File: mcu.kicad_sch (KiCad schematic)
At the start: 15 parts, among them U3 STM32L431CBT6

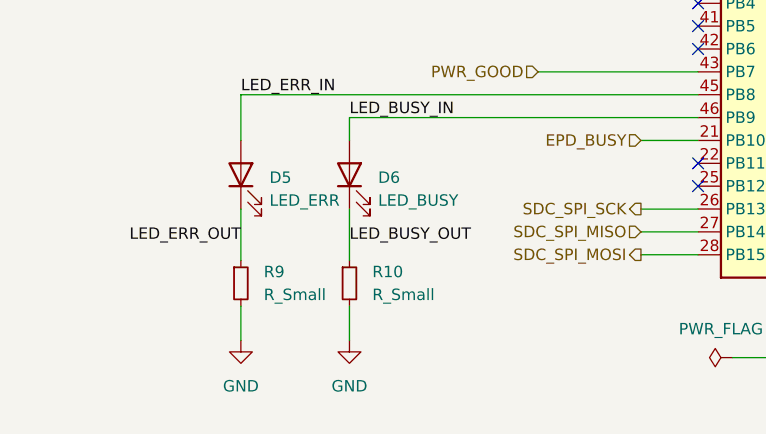
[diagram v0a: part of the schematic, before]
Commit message: Added footprint for components in Schematics. Updated LED resistors
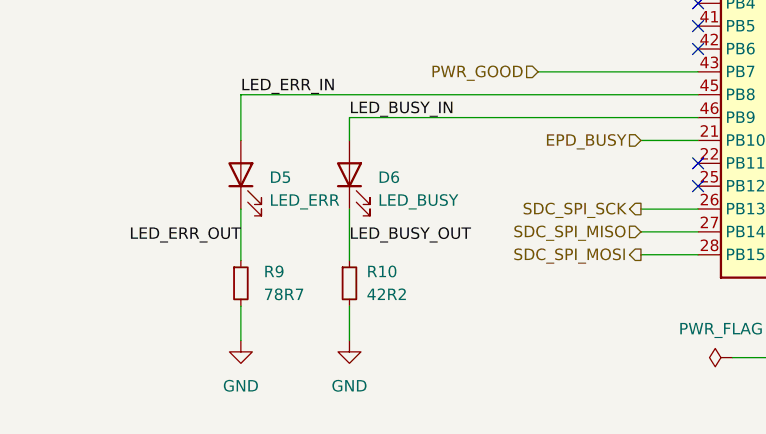
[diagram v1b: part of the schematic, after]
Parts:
- C37, C38, C39, C40, C41, C42, C43, C44: footprint (none) -> Capacitor_SMD:C_0201_0603Metric
- D5, D6: footprint (none) -> LED_THT:LED_D3.0mm
- L4: footprint (none) -> Inductor_SMD:L_0402_1005Metric
- R10: value R_Small -> 42R2; footprint (none) -> Resistor_SMD:R_1210_3225Metric
- R11: footprint (none) -> Resistor_SMD:R_0805_2012Metric
- R9: value R_Small -> 78R7; footprint (none) -> Resistor_SMD:R_1210_3225Metric
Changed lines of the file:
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@@
       (effects (font (size 1.27 1.27)) (justify left))
     )
-    (property "Footprint" "" (id 2) (at 143.51 40.64 0)
+    (property "Footprint" "Capacitor_SMD:C_0201_0603Metric" (id 2) (at 143.51 40.64 0)
       (effects (font (size 1.27 1.27)) hide)
     )
@@
       (effects (font (size 1.27 1.27)) (justify left))
     )
-    (property "Value" "R_Small" (id 1) (at 80.01 141.6049 0)
-      (effects (font (size 1.27 1.27)) (justify left))
-    )
-    (property "Footprint" "" (id 2) (at 77.47 140.335 0)
+    (property "Value" "78R7" (id 1) (at 80.01 141.6049 0)
+      (effects (font (size 1.27 1.27)) (justify left))
+    )
+    (property "Footprint" "Resistor_SMD:R_1210_3225Metric" (id 2) (at 77.47 140.335 0)
       (effects (font (size 1.27 1.27)) hide)
     )
@@
       (effects (font (size 1.27 1.27)) (justify left))
     )
-    (property "Footprint" "" (id 2) (at 110.49 40.64 0)
+    (property "Footprint" "Capacitor_SMD:C_0201_0603Metric" (id 2) (at 110.49 40.64 0)
       (effects (font (size 1.27 1.27)) hide)
     )
@@
       (effects (font (size 1.27 1.27)) (justify right))
     )
-    (property "Footprint" "" (id 2) (at 89.535 128.27 0)
+    (property "Footprint" "LED_THT:LED_D3.0mm" (id 2) (at 89.535 128.27 0)
       (effects (font (size 1.27 1.27)) hide)
     )
@@
       (effects (font (size 1.27 1.27)) (justify left))
     )
-    (property "Footprint" "" (id 2) (at 184.15 38.1 0)
+    (property "Footprint" "Capacitor_SMD:C_0201_0603Metric" (id 2) (at 184.15 38.1 0)
       (effects (font (size 1.27 1.27)) hide)
     )
@@
       (effects (font (size 1.27 1.27)) (justify right))
     )
-    (property "Footprint" "" (id 2) (at 77.47 128.27 0)
+    (property "Footprint" "LED_THT:LED_D3.0mm" (id 2) (at 77.47 128.27 0)
       (effects (font (size 1.27 1.27)) hide)
     )
@@
       (effects (font (size 1.27 1.27)) (justify left))
     )
-    (property "Footprint" "" (id 2) (at 132.08 40.64 0)
+    (property "Footprint" "Capacitor_SMD:C_0201_0603Metric" (id 2) (at 132.08 40.64 0)
       (effects (font (size 1.27 1.27)) hide)
     )
@@
       (effects (font (size 1.27 1.27)) (justify left))
     )
-    (property "Footprint" "" (id 2) (at 154.94 40.64 0)
+    (property "Footprint" "Capacitor_SMD:C_0201_0603Metric" (id 2) (at 154.94 40.64 0)
       (effects (font (size 1.27 1.27)) hide)
     )
@@
   (symbol (lib_id "Device:R_Small") (at 89.535 140.335 0) (unit 1)
     (in_bom yes) (on_board yes) (fields_autoplaced)
-    (property "Reference" "R10" (id 0) (at 92.075 139.0649 0)
-      (effects (font (size 1.27 1.27)) (justify left))
-    )
-    (property "Value" "R_Small" (id 1) (at 92.075 141.6049 0)
-      (effects (font (size 1.27 1.27)) (justify left))
-    )
-    (property "Footprint" "" (id 2) (at 89.535 140.335 0)
+    (property "Reference" "R10" (id 0) (at 91.44 139.0649 0)
+      (effects (font (size 1.27 1.27)) (justify left))
+    )
+    (property "Value" "42R2" (id 1) (at 91.44 141.6049 0)
+      (effects (font (size 1.27 1.27)) (justify left))
+    )
+    (property "Footprint" "Resistor_SMD:R_1210_3225Metric" (id 2) (at 89.535 140.335 0)
       (effects (font (size 1.27 1.27)) hide)
     )
@@
       (effects (font (size 1.27 1.27)) (justify left))
     )
-    (property "Footprint" "" (id 2) (at 101.6 88.265 0)
+    (property "Footprint" "Resistor_SMD:R_0805_2012Metric" (id 2) (at 101.6 88.265 0)
       (effects (font (size 1.27 1.27)) hide)
     )
@@
       (effects (font (size 1.27 1.27)) (justify left))
     )
-    (property "Footprint" "" (id 2) (at 120.65 40.64 0)
+    (property "Footprint" "Capacitor_SMD:C_0201_0603Metric" (id 2) (at 120.65 40.64 0)
       (effects (font (size 1.27 1.27)) hide)
     )
@@
       (effects (font (size 1.27 1.27)) (justify left))
     )
-    (property "Footprint" "" (id 2) (at 175.26 38.1 0)
+    (property "Footprint" "Capacitor_SMD:C_0201_0603Metric" (id 2) (at 175.26 38.1 0)
       (effects (font (size 1.27 1.27)) hide)
     )
@@
     (property "Reference" "L4" (id 0) (at 170.18 29.21 90))
     (property "Value" "39nH" (id 1) (at 170.18 31.75 90))
-    (property "Footprint" "" (id 2) (at 170.18 34.29 0)
+    (property "Footprint" "Inductor_SMD:L_0402_1005Metric" (id 2) (at 170.18 34.29 0)
       (effects (font (size 1.27 1.27)) hide)
     )
@@
       (effects (font (size 1.27 1.27)) (justify left))
     )
-    (property "Footprint" "" (id 2) (at 92.075 80.01 0)
-      (effects (font (size 1.27 1.27)) hide)
-    )
+    (property "Footprint" "Capacitor_SMD:C_0201_0603Metric" (id 2) (at 92.075 80.01 0)
+      (effects (font (size 1.27 1.27)) hide)
+    )

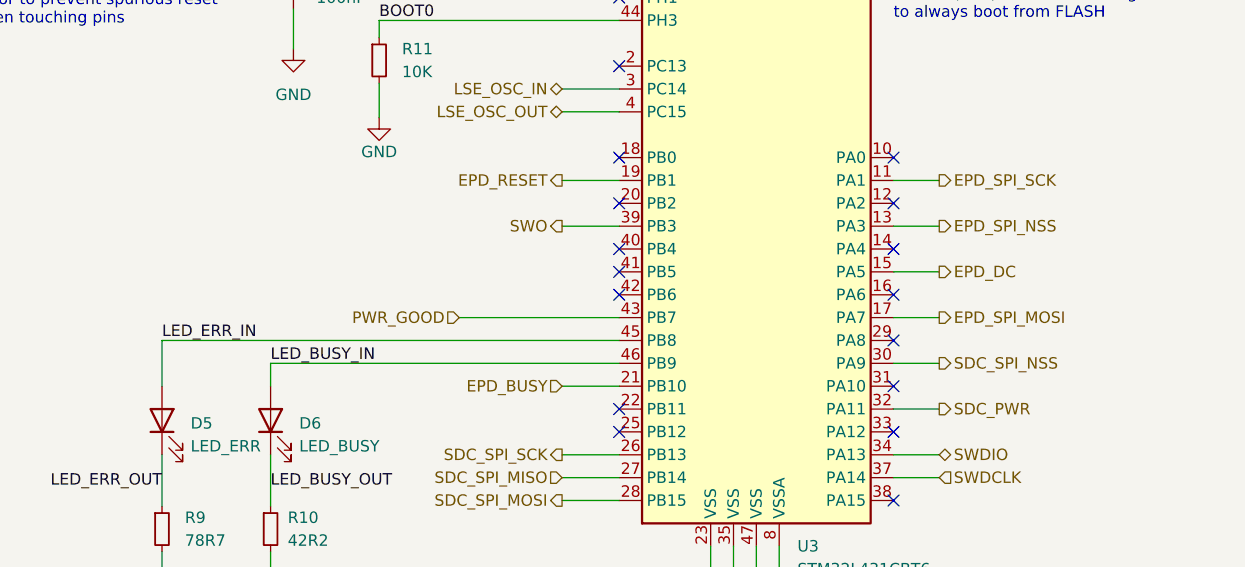
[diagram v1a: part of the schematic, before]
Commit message: Added preliminary PCL layout
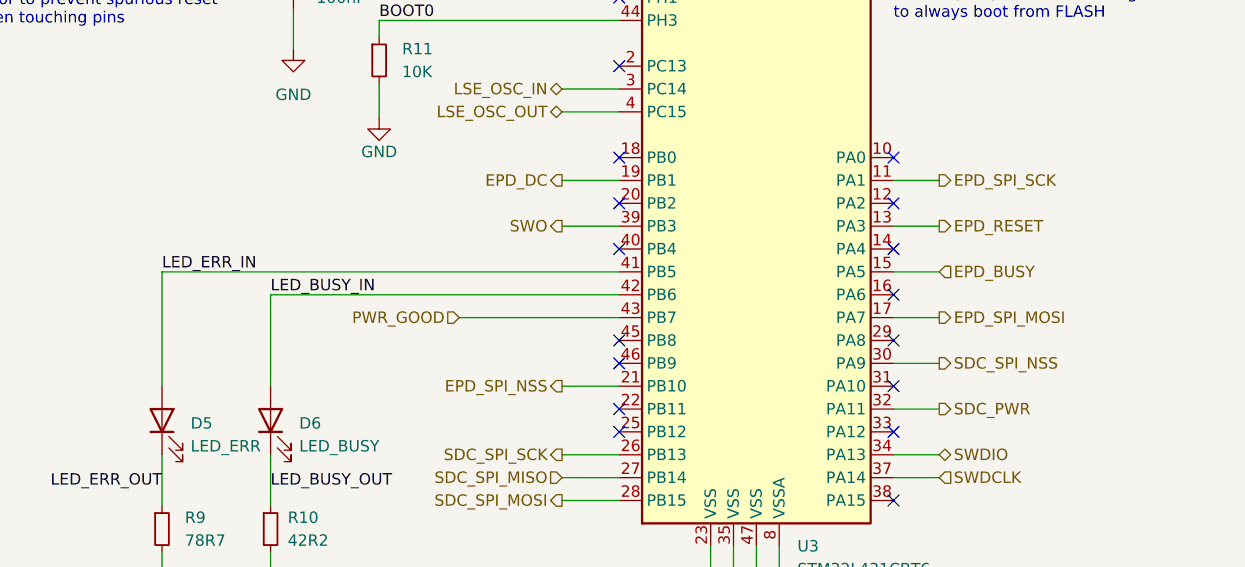
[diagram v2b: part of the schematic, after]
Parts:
- C37, C38, C39, C40, C41, C42, C43, C44: footprint Capacitor_SMD:C_0201_0603Metric -> Capacitor_SMD:C_0603_1608Metric
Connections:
- net EPD_BUSY: now also U3.15 (PA5); no longer U3.21 (PB10)
- net EPD_DC: now also U3.19 (PB1); no longer U3.15 (PA5)
- net EPD_RESET: now also U3.13 (PA3); no longer U3.19 (PB1)
- net EPD_SPI_NSS: now also U3.21 (PB10); no longer U3.13 (PA3)
- net LED_BUSY_IN: now also U3.42 (PB6); no longer U3.46 (PB9)
- net LED_ERR_IN: now also U3.41 (PB5); no longer U3.45 (PB8)
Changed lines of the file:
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@@
   (junction (at 140.97 146.05) (diameter 0) (color 0 0 0 0)
   )
+  (no_connect (at 128.27 121.92))
   (no_connect (at 158.75 129.54))
   (no_connect (at 128.27 99.06))
   (no_connect (at 128.27 129.54))
+  (no_connect (at 128.27 119.38))
   (no_connect (at 128.27 81.28))
   (no_connect (at 158.75 109.22))
@@
   (no_connect (at 158.75 119.38))
   (no_connect (at 128.27 88.9))
-  (no_connect (at 128.27 111.76))
-  (no_connect (at 128.27 114.3))
   (no_connect (at 128.27 127))
   (no_connect (at 128.27 109.22))
@@
     (stroke (width 0) (type default) (color 0 0 0 0))
   )
-  (wire (pts (xy 77.47 119.38) (xy 128.27 119.38))
+  (wire (pts (xy 77.47 111.76) (xy 128.27 111.76))
     (stroke (width 0) (type default) (color 0 0 0 0))
   )
@@
     (stroke (width 0) (type default) (color 0 0 0 0))
   )
-  (wire (pts (xy 89.535 121.92) (xy 128.27 121.92))
+  (wire (pts (xy 89.535 114.3) (xy 128.27 114.3))
     (stroke (width 0) (type default) (color 0 0 0 0))
   )
@@
     (stroke (width 0) (type default) (color 0 0 0 0))
   )
-  (wire (pts (xy 89.535 121.92) (xy 89.535 124.46))
+  (wire (pts (xy 89.535 114.3) (xy 89.535 124.46))
     (stroke (width 0) (type default) (color 0 0 0 0))
   )
@@
     (stroke (width 0) (type default) (color 0 0 0 0))
   )
-  (wire (pts (xy 77.47 119.38) (xy 77.47 124.46))
+  (wire (pts (xy 77.47 111.76) (xy 77.47 124.46))
     (stroke (width 0) (type default) (color 0 0 0 0))
   )
@@
     (effects (font (size 1.27 1.27)) (justify right bottom))
   )
-  (label "LED_ERR_IN" (at 77.47 119.38 0)
+  (label "LED_ERR_IN" (at 77.47 111.76 0)
     (effects (font (size 1.27 1.27)) (justify left bottom))
   )
@@
     (effects (font (size 1.27 1.27)) (justify left bottom))
   )
-  (label "LED_BUSY_IN" (at 89.535 121.92 0)
-    (effects (font (size 1.27 1.27)) (justify left bottom))
-  )
-  (hierarchical_label "EPD_SPI_NSS" (shape output) (at 163.83 106.68 0)
-    (effects (font (size 1.27 1.27)) (justify left))
+  (label "LED_BUSY_IN" (at 89.535 114.3 0)
+    (effects (font (size 1.27 1.27)) (justify left bottom))
+  )
+  (hierarchical_label "EPD_SPI_NSS" (shape output) (at 121.92 124.46 180)
+    (effects (font (size 1.27 1.27)) (justify right))
   )
   (hierarchical_label "SDC_SPI_NSS" (shape output) (at 163.83 121.92 0)
@@
     (effects (font (size 1.27 1.27)) (justify right))
   )
-  (hierarchical_label "EPD_RESET" (shape output) (at 121.92 101.6 180)
-    (effects (font (size 1.27 1.27)) (justify right))
-  )
-  (hierarchical_label "EPD_DC" (shape output) (at 163.83 111.76 0)
-    (effects (font (size 1.27 1.27)) (justify left))
+  (hierarchical_label "EPD_RESET" (shape output) (at 163.83 106.68 0)
+    (effects (font (size 1.27 1.27)) (justify left))
+  )
+  (hierarchical_label "EPD_DC" (shape output) (at 121.92 101.6 180)
+    (effects (font (size 1.27 1.27)) (justify right))
   )
   (hierarchical_label "SDC_SPI_MISO" (shape input) (at 121.92 134.62 180)
@@
     (effects (font (size 1.27 1.27)) (justify right))
   )
-  (hierarchical_label "EPD_BUSY" (shape input) (at 121.92 124.46 180)
-    (effects (font (size 1.27 1.27)) (justify right))
+  (hierarchical_label "EPD_BUSY" (shape input) (at 163.83 111.76 0)
+    (effects (font (size 1.27 1.27)) (justify left))
   )
   (symbol (lib_id "Device:C_Small") (at 143.51 40.64 0) (unit 1)
@@
       (effects (font (size 1.27 1.27)) (justify left))
     )
-    (property "Footprint" "Capacitor_SMD:C_0201_0603Metric" (id 2) (at 143.51 40.64 0)
+    (property "Footprint" "Capacitor_SMD:C_0603_1608Metric" (id 2) (at 143.51 40.64 0)
       (effects (font (size 1.27 1.27)) hide)
     )
@@
       (effects (font (size 1.27 1.27)) (justify left))
     )
-    (property "Footprint" "Capacitor_SMD:C_0201_0603Metric" (id 2) (at 110.49 40.64 0)
+    (property "Footprint" "Capacitor_SMD:C_0603_1608Metric" (id 2) (at 110.49 40.64 0)
       (effects (font (size 1.27 1.27)) hide)
     )
@@
       (effects (font (size 1.27 1.27)) (justify left))
     )
-    (property "Footprint" "Capacitor_SMD:C_0201_0603Metric" (id 2) (at 184.15 38.1 0)
+    (property "Footprint" "Capacitor_SMD:C_0603_1608Metric" (id 2) (at 184.15 38.1 0)
       (effects (font (size 1.27 1.27)) hide)
     )
@@
       (effects (font (size 1.27 1.27)) (justify left))
     )
-    (property "Footprint" "Capacitor_SMD:C_0201_0603Metric" (id 2) (at 132.08 40.64 0)
+    (property "Footprint" "Capacitor_SMD:C_0603_1608Metric" (id 2) (at 132.08 40.64 0)
       (effects (font (size 1.27 1.27)) hide)
     )
@@
       (effects (font (size 1.27 1.27)) (justify left))
     )
-    (property "Footprint" "Capacitor_SMD:C_0201_0603Metric" (id 2) (at 154.94 40.64 0)
+    (property "Footprint" "Capacitor_SMD:C_0603_1608Metric" (id 2) (at 154.94 40.64 0)
       (effects (font (size 1.27 1.27)) hide)
     )
@@
       (effects (font (size 1.27 1.27)) (justify left))
     )
-    (property "Footprint" "Capacitor_SMD:C_0201_0603Metric" (id 2) (at 120.65 40.64 0)
+    (property "Footprint" "Capacitor_SMD:C_0603_1608Metric" (id 2) (at 120.65 40.64 0)
       (effects (font (size 1.27 1.27)) hide)
     )
@@
       (effects (font (size 1.27 1.27)) (justify left))
     )
-    (property "Footprint" "Capacitor_SMD:C_0201_0603Metric" (id 2) (at 175.26 38.1 0)
+    (property "Footprint" "Capacitor_SMD:C_0603_1608Metric" (id 2) (at 175.26 38.1 0)
       (effects (font (size 1.27 1.27)) hide)
     )
@@
       (effects (font (size 1.27 1.27)) (justify left))
     )
-    (property "Footprint" "Capacitor_SMD:C_0201_0603Metric" (id 2) (at 92.075 80.01 0)
-      (effects (font (size 1.27 1.27)) hide)
-    )
+    (property "Footprint" "Capacitor_SMD:C_0603_1608Metric" (id 2) (at 92.075 80.01 0)
+      (effects (font (size 1.27 1.27)) hide)
+    )

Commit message: Revision 1 of the board that was manufactured
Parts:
- added R12: 5k, Resistor_SMD:R_1206_3216Metric, symbol Device:R_Small
- C37, C39, C40, C41, C42: LCSC (none) -> C14663
- C38: LCSC (none) -> C19666
- C43: LCSC (none) -> C15849
- C44: LCSC (none) -> C57112
- L4: LCSC (none) -> C440213
- R10: value 42R2 -> 47k; LCSC (none) -> C230465
- R11: LCSC (none) -> C510098
- R9: value 78R7 -> 47k; LCSC (none) -> C230465
- U3: LCSC (none) -> C277951
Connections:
- net GND: now also R12.2; no longer R10.2
- new net LED_BUSY_OUT_2: R10.2, R12.1
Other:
- moved on the sheet: C37, D5, D6, R10, R11, R9
